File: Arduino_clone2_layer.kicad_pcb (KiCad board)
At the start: 2 copper layers, 41 x 30 mm, 17 parts, among them J1 Conn_01x04, J2 DIGITAL PIN, J3 Conn_01x04, J4 icsp, U1 DS1337_ben, U2 24LC1025, U3 24LC1025, U4 ATmega328P-A, Y1 Crystal, Y2 Crystal

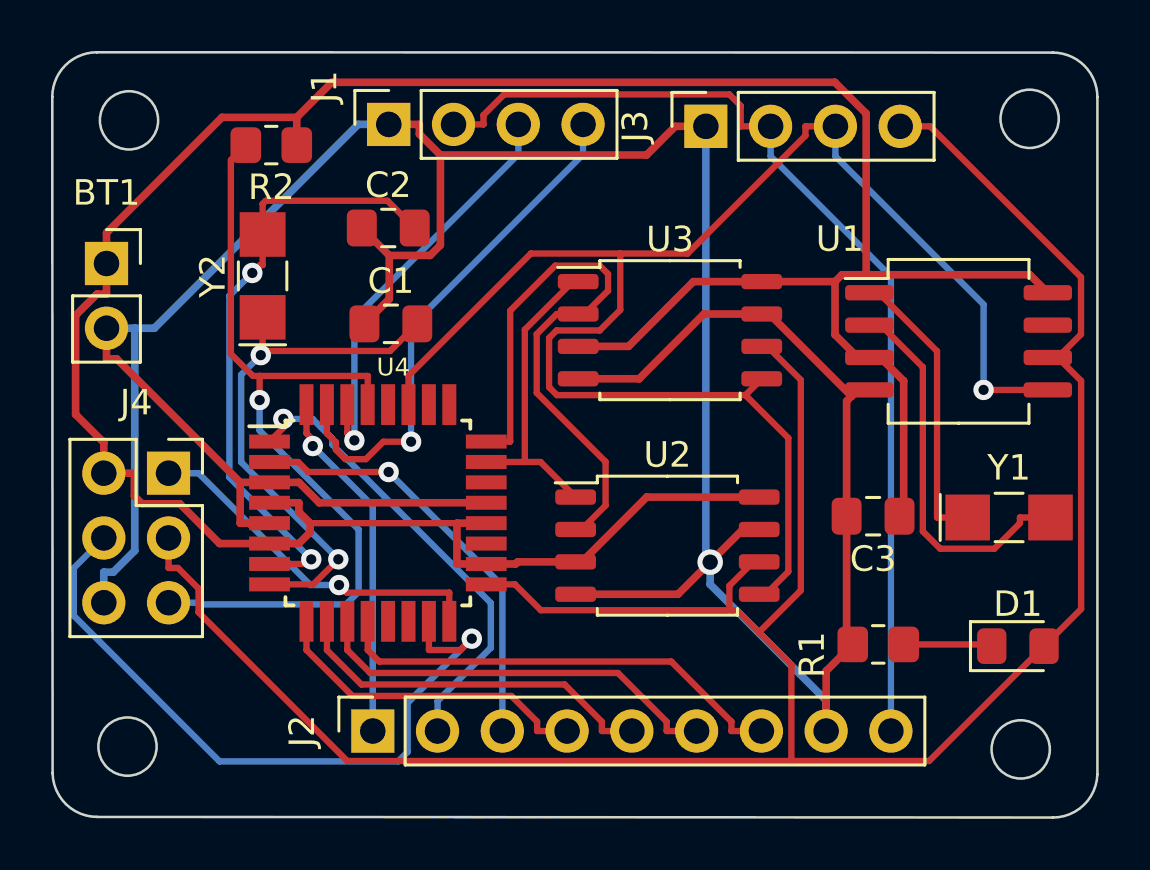
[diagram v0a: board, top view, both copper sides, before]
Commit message: copper fillxone on the 2layer boared
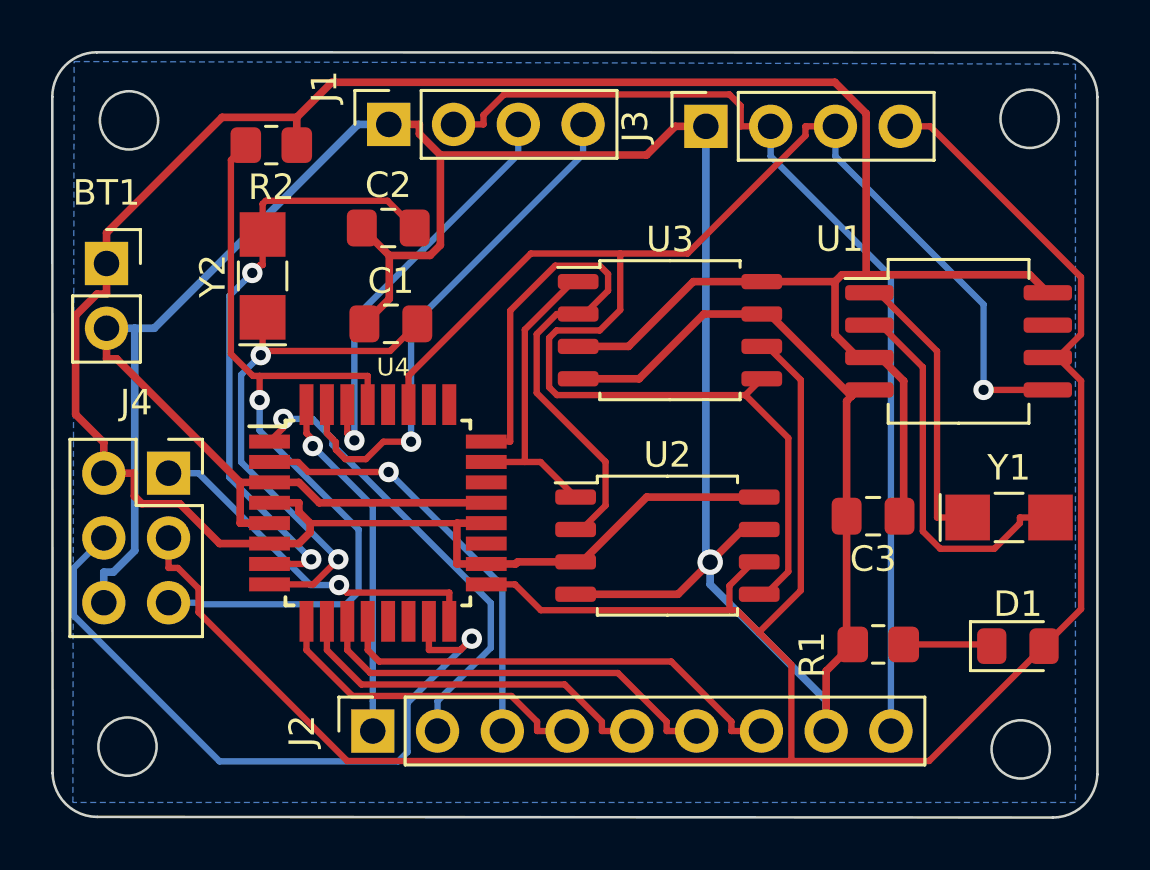
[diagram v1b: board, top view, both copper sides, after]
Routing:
- added copper zone on B.Cu, net GNDPWR
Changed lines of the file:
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@@
   (segment (start 134.1728 95.0795) (end 138.89 99.7967) (width 0.25) (layer "B.Cu") (net 32))
   (segment (start 138.89 99.7967) (end 138.89 117.62) (width 0.25) (layer "B.Cu") (net 32))
+  (zone (net 2) (net_name "GNDPWR") (layer "B.Cu") (hatch edge 0.508)
+    (connect_pads (clearance 0.508))
+    (min_thickness 0.254) (filled_areas_thickness no)
+    (fill yes (thermal_gap 0.508) (thermal_bridge_width 0.508))
+    (polygon
+      (pts
+        (xy 146.1262 91.4654)
+        (xy 146.1262 120.4214)
+        (xy 106.807 120.4214)
+        (xy 106.8578 91.3638)
+      )
+    )
+  )
 )

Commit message: complete work on 2 layer boared added silkscreen
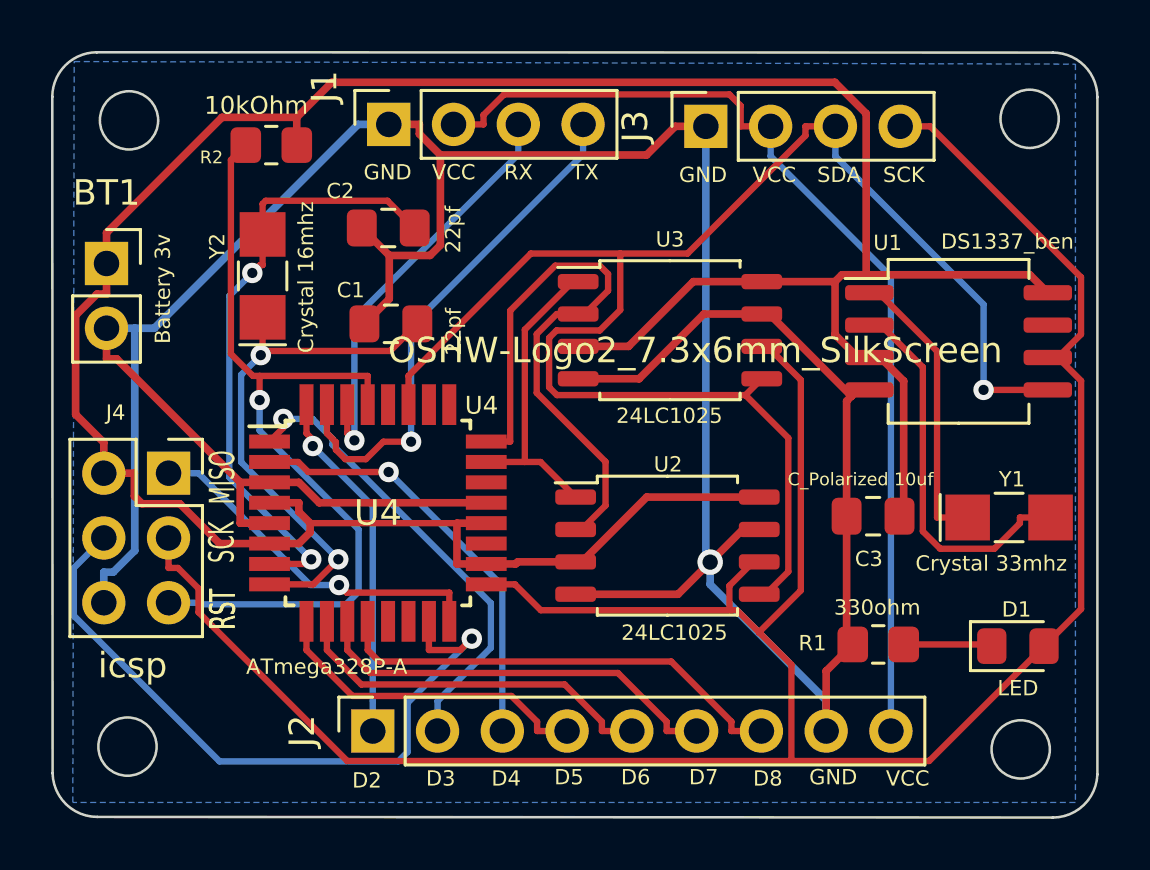
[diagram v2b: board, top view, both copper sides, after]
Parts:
- added REF**: KiCad-Logo2_6mm_SilkScreen, Symbol:KiCad-Logo2_6mm_SilkScreen, B.Cu at (116.7, 106.1)
- added REF**: OSHW-Logo2_7.3x6mm_SilkScreen, Symbol:OSHW-Logo2_7.3x6mm_SilkScreen, B.Cu at (129.8, 98.0)
- J1, J3: value Conn_01x04 -> GND
- J2: value DIGITAL PIN -> D2
- R2: value R -> 10kOhm
- Y1: value Crystal -> Crystal 33mhz
- Y2: value Crystal -> Crystal 16mhz
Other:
- board text added: "Arduino clone with: -2Mbit EEPROM -Clock & Calender -I2C, SPI, GPIO Designed by Bernard"
- board text added: "MISO"
- board text added: "RST"
- board text added: "SCK"
